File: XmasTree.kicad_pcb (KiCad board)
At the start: 2 copper layers, 80.7 x 95.9 mm, 0 parts

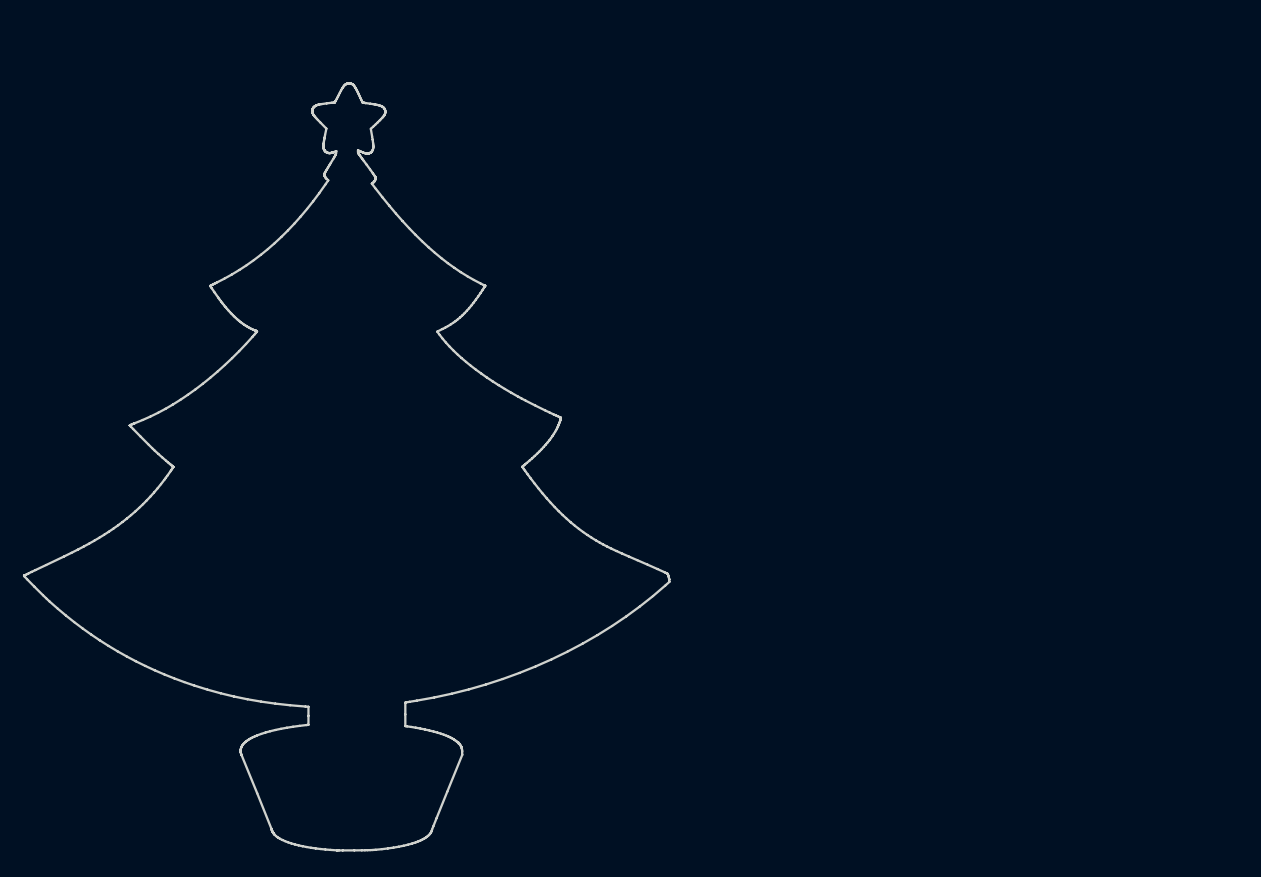
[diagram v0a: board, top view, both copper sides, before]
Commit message: Start laying out pcb
Signed-off-by: Giuseppe Barillari <joe2k01dev@gmail.com>
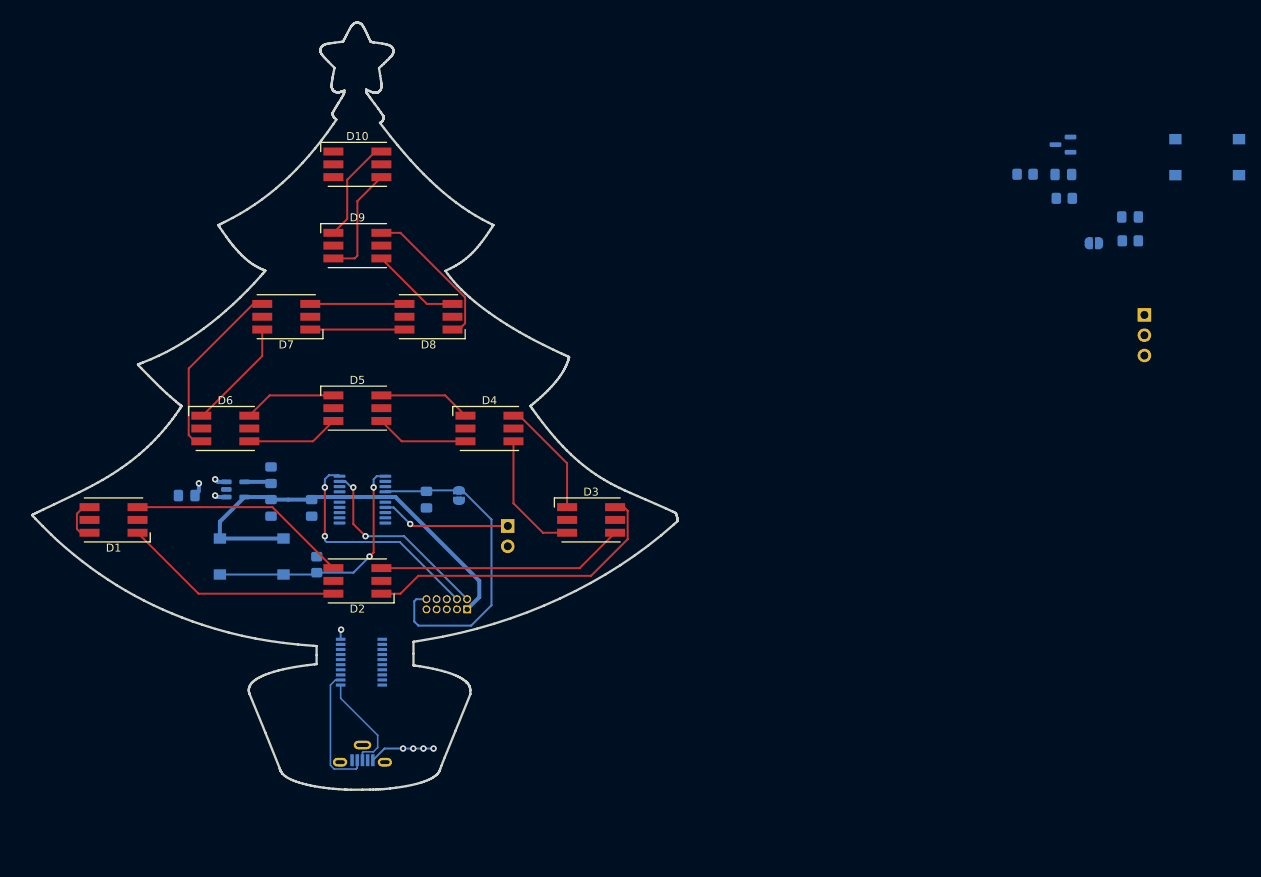
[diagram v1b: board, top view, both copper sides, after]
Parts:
- added C1: 10n, Capacitor_SMD:C_0805_2012Metric_Pad1.18x1.45mm_HandSolder, B.Cu at (144.1, 33.0)
- added C2: 1u, Capacitor_SMD:C_0805_2012Metric_Pad1.18x1.45mm_HandSolder, B.Cu at (34.5, 73.2)
- added C3: 10n, Capacitor_SMD:C_0805_2012Metric_Pad1.18x1.45mm_HandSolder, B.Cu at (45.1, 70.6)
- added C4: 1u, Capacitor_SMD:C_0805_2012Metric_Pad1.18x1.45mm_HandSolder, B.Cu at (45.1, 74.7)
- added C5: 10n, Capacitor_SMD:C_0805_2012Metric_Pad1.18x1.45mm_HandSolder, B.Cu at (50.2, 74.7)
- added C6: 4u7, Capacitor_SMD:C_0805_2012Metric_Pad1.18x1.45mm_HandSolder, B.Cu at (152.5, 38.3)
- added C7: 10n, Capacitor_SMD:C_0805_2012Metric_Pad1.18x1.45mm_HandSolder, B.Cu at (64.5, 73.7)
- added D1: WS2813B, Library:LED_WS2813_hand, F.Cu at (25.4, 76.2)
- added D10: WS2813B, Library:LED_WS2813_hand, F.Cu at (55.9, 31.8)
- added D2: WS2813B, Library:LED_WS2813_hand, F.Cu at (55.9, 83.8)
- added D3: WS2813B, Library:LED_WS2813_hand, F.Cu at (85.1, 76.2)
- added D4: WS2813B, Library:LED_WS2813_hand, F.Cu at (72.4, 64.8)
- added D5: WS2813B, Library:LED_WS2813_hand, F.Cu at (55.9, 62.2)
- added D6: WS2813B, Library:LED_WS2813_hand, F.Cu at (39.4, 64.8)
- added D7: WS2813B, Library:LED_WS2813_hand, F.Cu at (47.0, 50.8)
- added D8: WS2813B, Library:LED_WS2813_hand, F.Cu at (64.8, 50.8)
- added D9: WS2813B, Library:LED_WS2813_hand, F.Cu at (55.9, 41.9)
- added J1: USB_B_Micro, Connector_USB:USB_Micro-B_Molex-105133-0001, B.Cu at (56.5, 105.4)
- added J2: Conn_ARM_JTAG_SWD_10, Connector_PinHeader_1.27mm:PinHeader_2x05_P1.27mm_Vertical, B.Cu at (69.6, 87.4)
- added J3: Conn_01x03_Male, Connector_PinHeader_2.54mm:PinHeader_1x03_P2.54mm_Vertical, B.Cu at (154.3, 50.6)
- added J4: Conn_01x02_Male, Connector_PinHeader_2.54mm:PinHeader_1x02_P2.54mm_Vertical, B.Cu at (74.7, 77.0)
- added JP1: SolderJumper_2_Open, Jumper:SolderJumper-2_P1.3mm_Open_RoundedPad1.0x1.5mm, B.Cu at (147.9, 41.6)
- added JP2: SolderJumper_2_Open, Jumper:SolderJumper-2_P1.3mm_Open_RoundedPad1.0x1.5mm, B.Cu at (68.6, 73.2)
- added Q1: BSN20, Package_TO_SOT_SMD:SOT-23, B.Cu at (144.1, 29.3)
- added R1: 10k, Resistor_SMD:R_0805_2012Metric_Pad1.20x1.40mm_HandSolder, B.Cu at (139.3, 33.0)
- added R2: 10k, Resistor_SMD:R_0805_2012Metric_Pad1.20x1.40mm_HandSolder, B.Cu at (144.2, 36.0)
- added R3: 10k, Resistor_SMD:R_0805_2012Metric_Pad1.20x1.40mm_HandSolder, B.Cu at (152.5, 41.3)
- added R4: 10k, Resistor_SMD:R_0805_2012Metric_Pad1.20x1.40mm_HandSolder, B.Cu at (50.8, 81.8)
- added SW1: SW_Push, Button_Switch_SMD:SW_Push_1P1T_NO_6x6mm_H9.5mm, B.Cu at (162.1, 30.9)
- added SW2: SW_Push, Button_Switch_SMD:SW_Push_1P1T_NO_6x6mm_H9.5mm, B.Cu at (42.7, 80.8)
- added U1: FT231XS, Package_SO:SSOP-20_3.9x8.7mm_P0.635mm, B.Cu at (56.4, 94.0)
- added U2: AP2202K-3.3, Package_TO_SOT_SMD:SOT-23-5, B.Cu at (40.6, 72.4)
- added U3: STM32L011F4Px, Package_SO:TSSOP-20_4.4x6.5mm_P0.65mm, B.Cu at (56.5, 73.7)
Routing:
- net +3.3V: track 0.00 -> 53.2 mm
- net /3v3 MCU/rst: track 0.00 -> 40.7 mm
- net Net-(D2-Pad1): track 0.00 -> 38.9 mm
- net Net-(U3-Pad1): track 0.00 -> 31.2 mm, vias 0 -> 2
- net Net-(D2-Pad3): track 0.00 -> 31.0 mm
- net /3v3 MCU/swclk: track 0.00 -> 29.3 mm, vias 0 -> 2
- net Net-(D1-Pad3): track 0.00 -> 27.6 mm
- net Net-(D1-Pad1): track 0.00 -> 27.6 mm
- net /3v3 MCU/swdio: track 0.00 -> 24.5 mm, vias 0 -> 2
- net Net-(D6-Pad3): track 0.00 -> 22.8 mm
- net Net-(D8-Pad1): track 0.00 -> 18.9 mm
- net Net-(J4-Pad1): track 0.00 -> 16.3 mm, vias 0 -> 1
- net /UsbD-: track 0.00 -> 16.1 mm
- net Net-(D3-Pad3): track 0.00 -> 16.0 mm
- net Net-(D3-Pad1): track 0.00 -> 14.6 mm
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
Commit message: RC 1
Signed-off-by: Giuseppe Barillari <joe2k01dev@gmail.com>
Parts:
- SW1: moved to F.Cu
- moved R3 134.2 mm to (23.9, 79.8), turned to 0 degrees
- moved SW1 129.4 mm to (40.1, 74.2)
- moved Q1 126.5 mm to (29.0, 81.8)
- moved R2 120.2 mm to (33.5, 82.8)
- moved J3 118.8 mm to (46.2, 100.1), turned to -90 degrees
- moved C1 118.8 mm to (49.8, 105.2), turned to 90 degrees
- moved JP1 106.9 mm to (58.4, 100.1)
- moved R1 105.1 mm to (56.4, 97.5), turned to 0 degrees
- moved C6 99.1 mm to (62.5, 79.8), turned to 0 degrees
- moved J2 44.0 mm to (29.3, 69.9), turned to -45 degrees
- moved J4 32.4 mm to (42.7, 81.8), turned to -90 degrees
- moved C2 28.1 mm to (62.5, 76.2), turned to 0 degrees
- moved C7 22.4 mm to (42.2, 72.1), turned to 90 degrees
- moved JP2 21.3 mm to (47.2, 72.6), turned to 90 degrees
- moved U3 20.1 mm to (36.6, 76.2)
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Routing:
- net /3v3 MCU/UartRX: track 1.23 -> 40.1 mm, vias 1 -> 2
- net /3v3 MCU/UartTX: track 0.00 -> 38.8 mm, vias 0 -> 1
- net /3v3 MCU/swclk: track 29.3 -> 4.44 mm, vias 2 -> 0
- net +5V: track 5.01 -> 29.3 mm, vias 3 -> 10
- net GND: track 8.19 -> 30.1 mm, vias 4 -> 16
- net /3v3 MCU/rst: track 40.7 -> 20.1 mm
- net /3v3 MCU/swdio: track 24.5 -> 5.41 mm, vias 2 -> 0
- net +3.3V: track 53.2 -> 69.8 mm
- net Net-(U3-Pad1): track 31.2 -> 15.3 mm, vias 2 -> 0
- net /3v3 MCU/btnA: track 0.00 -> 12.9 mm, vias 0 -> 1
- net Net-(C1-Pad1): track 0.00 -> 12.1 mm
- net Net-(J4-Pad1): track 16.3 -> 6.36 mm, vias 1 -> 0
- net /pxCtrlLV: track 0.00 -> 9.19 mm
- net /neopixel string/pxCtrl: track 5.60 -> 13.1 mm, vias 0 -> 1
- net Net-(U1-Pad13): track 0.00 -> 6.89 mm, vias 0 -> 2
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- added copper zone on B.Cu, net +5V
- added copper zone on F.Cu, net GND

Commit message: Review. Set USB as differential pair. Implemented USB-UART as in Data Sheet application circuit.
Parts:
- removed R1: 10k, Resistor_SMD:R_0805_2012Metric_Pad1.20x1.40mm_HandSolder
- added C8: 10n, Capacitor_SMD:C_0805_2012Metric_Pad1.18x1.45mm_HandSolder, B.Cu at (53.3, 94.0)
- added C9: 1u, Capacitor_SMD:C_0805_2012Metric_Pad1.18x1.45mm_HandSolder, B.Cu at (53.3, 89.9)
- added R5: 27, Resistor_SMD:R_0805_2012Metric_Pad1.20x1.40mm_HandSolder, B.Cu at (57.1, 98.3)
- added R6: 27, Resistor_SMD:R_0805_2012Metric_Pad1.20x1.40mm_HandSolder, B.Cu at (55.1, 98.3)
- JP1: moved to F.Cu
- moved J3 13.9 mm to (44.0, 86.4)
- moved C1 12.4 mm to (62.2, 105.4), turned to -90 degrees
- moved JP1 2.65 mm to (56.2, 98.6), turned to 0 degrees
- moved U1 1.80 mm to (58.2, 91.7), turned to 180 degrees
- moved J1 0.13 mm to (56.6, 105.5), turned to 180 degrees
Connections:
- U1 pad 11: /UsbD+ -> Net-(U1-Pad11)
- U1 pad 12: /UsbD- -> Net-(U1-Pad12)
- U1 pad 14: Net-(R1-Pad2) -> Net-(U1-Pad13)
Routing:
- net /3v3 MCU/UartRX: track 40.1 -> 29.0 mm, vias 2 -> 1
- net Net-(C1-Pad1): track 12.1 -> 2.79 mm
- net /3v3 MCU/UartTX: track 38.8 -> 31.2 mm
- net /UsbD-: track 13.7 -> 6.90 mm, vias 0 -> 1
- net /UsbD+: track 13.5 -> 6.92 mm, vias 0 -> 1
- net +5V: track 29.3 -> 22.8 mm, vias 10 -> 12
- net Net-(U1-Pad13): track 6.89 -> 13.1 mm, vias 2 -> 0
- net Net-(U1-Pad12): track 0.00 -> 4.44 mm
- net Net-(R1-Pad2): track 3.02 -> 0.00 mm
- net Net-(D6-Pad1): track 14.0 -> 17.0 mm
- net Net-(U1-Pad11): track 0.00 -> 2.90 mm
- net Net-(D2-Pad3): track 31.0 -> 32.9 mm
- net Net-(D8-Pad3): track 11.2 -> 12.1 mm
- net Net-(D10-Pad4): track 14.2 -> 15.0 mm
- net Net-(D3-Pad3): track 16.0 -> 15.3 mm
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- added copper zone on B.Cu, net Net-(C1-Pad1)
- added copper zone on F.Cu, net Net-(C1-Pad1)
